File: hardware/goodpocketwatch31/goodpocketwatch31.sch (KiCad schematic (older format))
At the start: 23 parts, among them J1 ANT_U.FL, U1 CC430F613x, U2 0915LP15B02, U3 B0310J50100AHF, Y1 32.768kHz, Y2 FA128 26MHz

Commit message: Bit more drafting, almost done with the pocket watch. #147
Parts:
- added BT1, BT2: AAAA, goodpocketwatch31:BE-AAAA-PC, symbol Device:Battery_Cell
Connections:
- net GND: now also BT2.2 (-)
- net VCC: now also BT1.1 (+)
- new net: BT1.2 (-), BT2.1 (+)
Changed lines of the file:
@@
 Wire Wire Line
 	5450 6400 5450 6500
-$Comp
-L Device:Buzzer BZ1
-U 1 1 5FEB8753
-P 10500 3150
-F 0 "BZ1" H 10652 3179 50  0000 L CNN
-F 1 "Buzzer" H 10652 3088 50  0000 L CNN
-F 2 "goodpocketwatch31:PT-1203-3" V 10475 3250 50  0001 C CNN
-F 3 "~" V 10475 3250 50  0001 C CNN
-	1    10500 3150
-	1    0    0    -1
-$EndComp
 Wire Wire Line
 	10400 3050 10100 3050
@@
 Text Notes 9750 5900 0    60   ~ 0
 Pushbutton rebuild of the\n4x4 watch keypad.
+$Comp
+L Device:Buzzer BZ1
+U 1 1 5FEB8753
+P 10500 3150
+F 0 "BZ1" H 10652 3179 50  0000 L CNN
+F 1 "Buzzer" H 10652 3088 50  0000 L CNN
+F 2 "goodpocketwatch31:PT-1203-3" V 10475 3250 50  0001 C CNN
+F 3 "~" V 10475 3250 50  0001 C CNN
+	1    10500 3150
+	1    0    0    -1
+$EndComp
+$Comp
+L Device:Battery_Cell BT1
+U 1 1 5FF1D008
+P 7400 4750
+F 0 "BT1" H 7518 4846 50  0000 L CNN
+F 1 "AAAA" H 7518 4755 50  0000 L CNN
+F 2 "goodpocketwatch31:BE-AAAA-PC" V 7400 4810 50  0001 C CNN
+F 3 "~" V 7400 4810 50  0001 C CNN
+	1    7400 4750
+	1    0    0    -1
+$EndComp
+$Comp
+L Device:Battery_Cell BT2
+U 1 1 5FF1D4A0
+P 7400 5200
+F 0 "BT2" H 7518 5296 50  0000 L CNN
+F 1 "AAAA" H 7518 5205 50  0000 L CNN
+F 2 "goodpocketwatch31:BE-AAAA-PC" V 7400 5260 50  0001 C CNN
+F 3 "~" V 7400 5260 50  0001 C CNN
+	1    7400 5200
+	1    0    0    -1
+$EndComp
+Wire Wire Line
+	7400 5000 7400 4850
+$Comp
+L power:GND #PWR024
+U 1 1 5FF2712A
+P 7400 5400
+F 0 "#PWR024" H 7400 5150 50  0001 C CNN
+F 1 "GND" H 7400 5250 50  0000 C CNN
+F 2 "" H 7400 5400 50  0000 C CNN
+F 3 "" H 7400 5400 50  0000 C CNN
+	1    7400 5400
+	1    0    0    -1
+$EndComp
+Wire Wire Line
+	7400 5400 7400 5300
+$Comp
+L power:VCC #PWR023
+U 1 1 5FF30EE9
+P 7400 4450
+F 0 "#PWR023" H 7400 4300 50  0001 C CNN
+F 1 "VCC" H 7400 4600 50  0000 C CNN
+F 2 "" H 7400 4450 50  0000 C CNN
+F 3 "" H 7400 4450 50  0000 C CNN
+	1    7400 4450
+	1    0    0    -1
+$EndComp
+Wire Wire Line
+	7400 4550 7400 4450
 $EndSCHEMATC

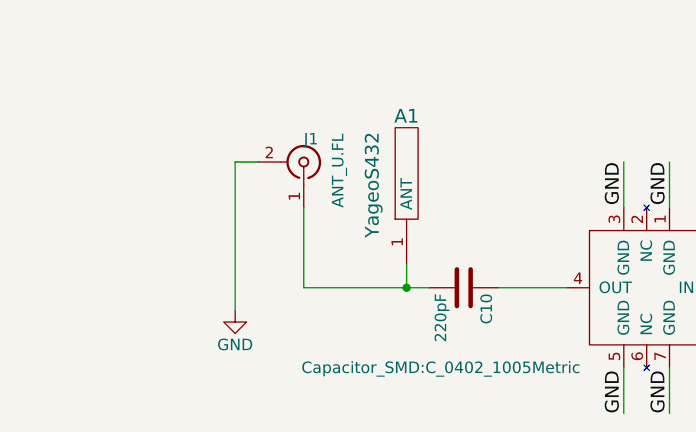
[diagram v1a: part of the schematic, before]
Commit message: Adds an edge-mount SMA connector, handy for RF accessories. #147
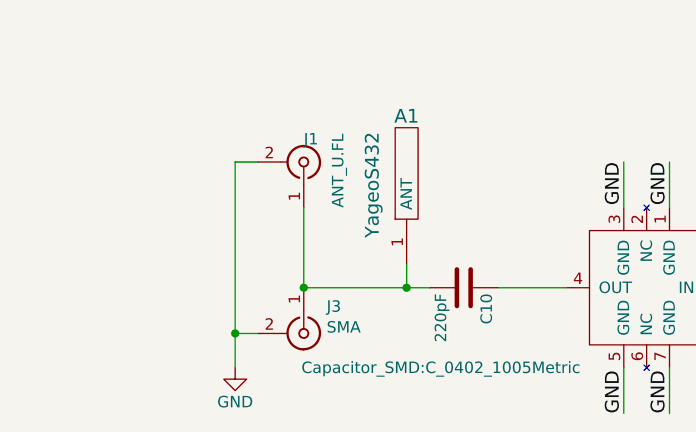
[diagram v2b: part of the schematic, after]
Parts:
- added J3: SMA, Connector_Coaxial:SMA_Amphenol_132289_EdgeMount, symbol Connector:Conn_Coaxial
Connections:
- net GND: now also J3.2 (Ext)
- net at A1.1 (ANT), C10.2, J1.1 (In): now also J3.1 (In)
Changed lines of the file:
@@
 Wire Wire Line
 	2800 7100 2350 7100
-Wire Wire Line
-	2350 7100 2350 6750
 Connection ~ 2800 7100
 $Comp
 L power:GND #PWR0101
 U 1 1 5B8FCF2F
-P 2050 7200
-F 0 "#PWR0101" H 2050 6950 50  0001 C CNN
-F 1 "GND" H 2050 7050 50  0000 C CNN
-F 2 "" H 2050 7200 50  0000 C CNN
-F 3 "" H 2050 7200 50  0000 C CNN
-	1    2050 7200
+P 2050 7450
+F 0 "#PWR0101" H 2050 7200 50  0001 C CNN
+F 1 "GND" H 2050 7300 50  0000 C CNN
+F 2 "" H 2050 7450 50  0000 C CNN
+F 3 "" H 2050 7450 50  0000 C CNN
+	1    2050 7450
 	1    0    0    -1
 $EndComp
 Wire Wire Line
 	2150 6550 2050 6550
-Wire Wire Line
-	2050 6550 2050 7200
 Text Label 5100 6100 0    60   ~ 0
 RFVCC
@@
 Wire Wire Line
 	7400 4550 7400 4450
+$Comp
+L Connector:Conn_Coaxial J3
+U 1 1 5FEB6E2D
+P 2350 7300
+F 0 "J3" V 2232 7400 50  0000 L CNN
+F 1 "SMA" V 2323 7400 50  0000 L CNN
+F 2 "Connector_Coaxial:SMA_Amphenol_132289_EdgeMount" H 2350 7300 50  0001 C CNN
+F 3 " ~" H 2350 7300 50  0001 C CNN
+	1    2350 7300
+	0    1    1    0
+$EndComp
+Wire Wire Line
+	2050 6550 2050 7300
+Wire Wire Line
+	2150 7300 2050 7300
+Connection ~ 2050 7300
+Wire Wire Line
+	2050 7300 2050 7450
+Wire Wire Line
+	2350 6750 2350 7100
+Connection ~ 2350 7100
 $EndSCHEMATC
